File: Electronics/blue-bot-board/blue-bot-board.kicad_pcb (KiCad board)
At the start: 2 copper layers, 65 x 100 mm, 16 parts, among them J1 5V PS, J12 I2C0, J13 Extra GPIO, J2 X, J3 Y, J4 Z, J5 X Limit Switch, J6 Y Limit Switch, J7 Z Limit Switch, J8 Servo, SW1 RESET

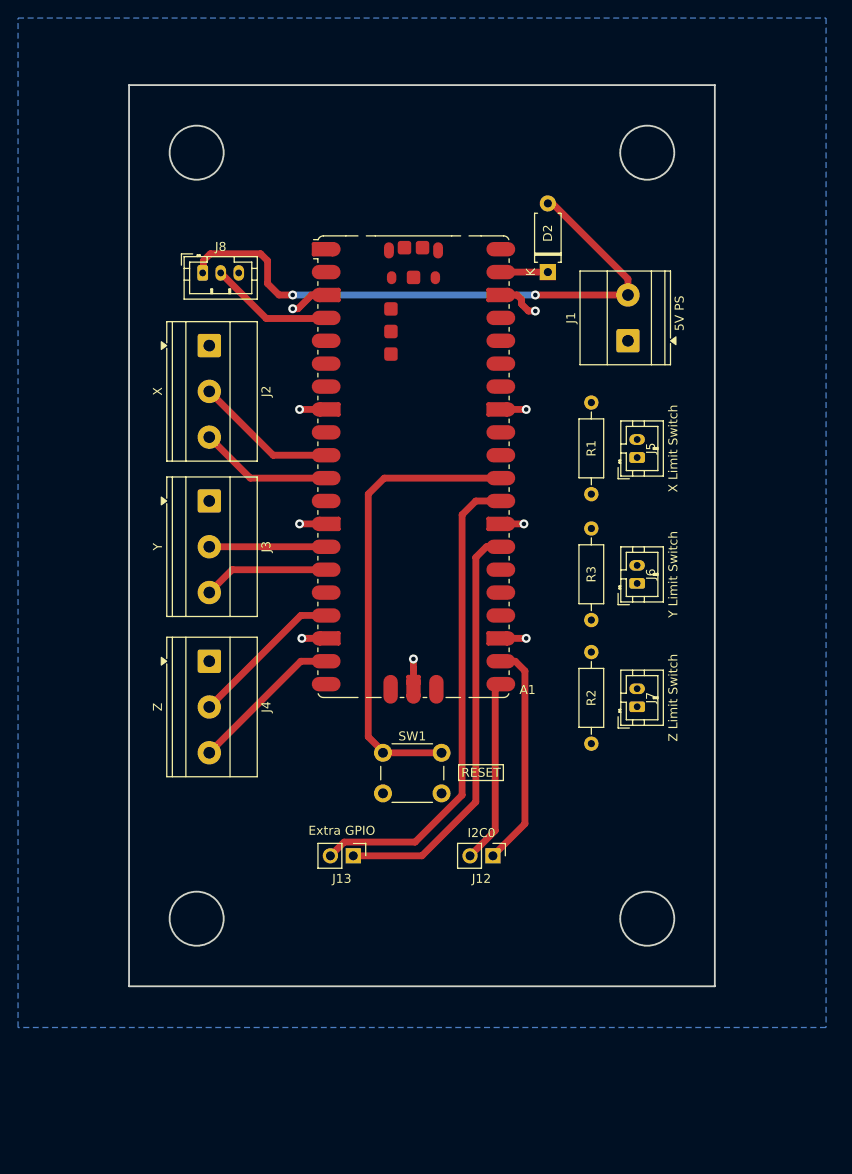
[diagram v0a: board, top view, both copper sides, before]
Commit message: Update PCB to production
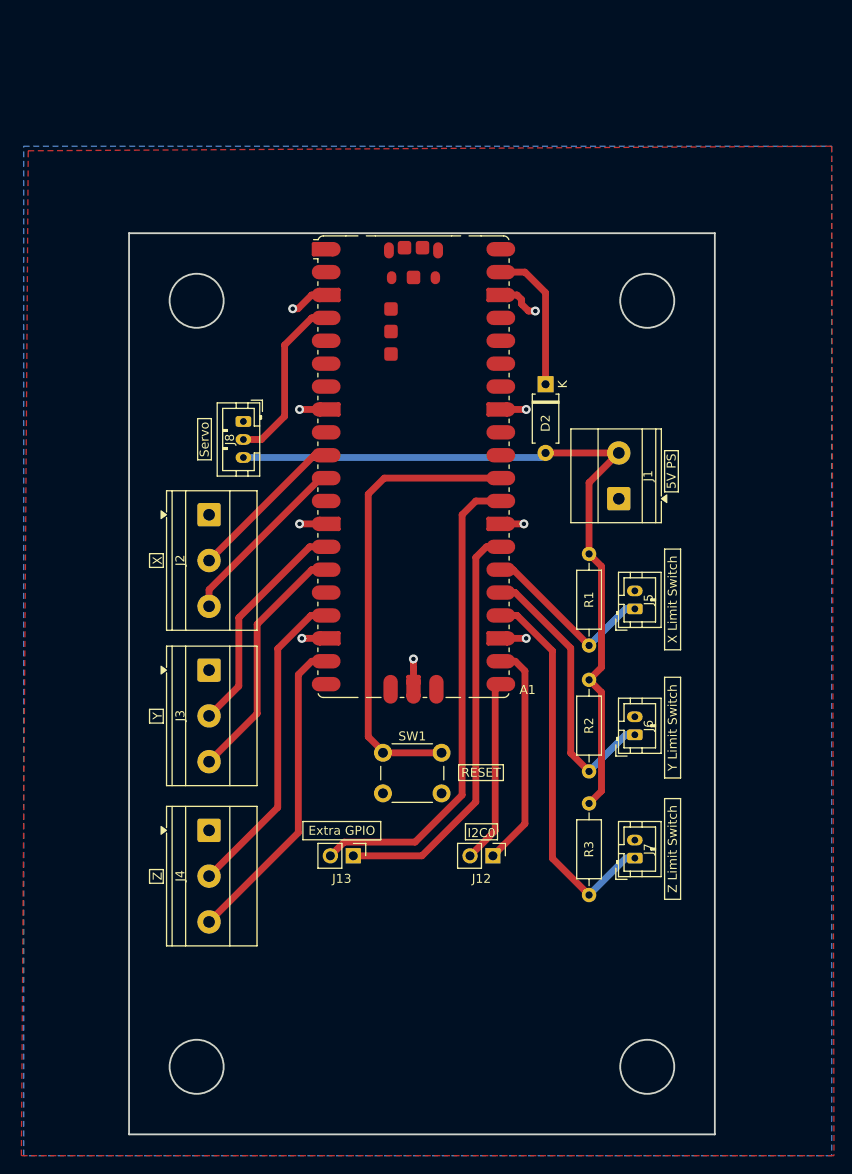
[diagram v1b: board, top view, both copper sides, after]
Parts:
- moved R3 30.5 mm to (164.1, 119.4)
- moved J2 18.8 mm to (121.9, 87.4)
- moved J3 18.8 mm to (121.9, 104.6)
- moved J4 18.8 mm to (121.9, 122.4)
- moved J1 17.6 mm to (167.4, 85.6)
- moved J8 17.1 mm to (125.7, 77.0), turned to -90 degrees
- moved J5 16.8 mm to (169.2, 97.8)
- moved J6 16.8 mm to (169.2, 111.8)
- moved J7 16.8 mm to (169.2, 125.5)
- moved R1 16.8 mm to (164.1, 91.7)
- moved D2 12.4 mm to (159.3, 72.9), turned to -90 degrees
- moved R2 3.09 mm to (164.1, 105.7)
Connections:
- J8 pad 1: +5V -> GND
- J8 pad 3: GND -> +5V
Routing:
- net Net-(A1-GPIO18): track 0.00 -> 42.9 mm
- net Net-(A1-GPIO19): track 0.00 -> 31.6 mm
- net Net-(A1-GPIO20): track 0.00 -> 20.0 mm
- net /GPIO13: track 17.2 -> 35.3 mm
- net /GPIO14: track 17.2 -> 35.2 mm
- net +5V: track 67.1 -> 84.4 mm, vias 2 -> 0
- net /GPIO11: track 14.0 -> 27.6 mm
- net /GPIO10: track 13.0 -> 25.2 mm
- net VCC: track 5.22 -> 16.4 mm
- net /GPIO2: track 13.8 -> 19.4 mm
- net /GPIO8: track 14.9 -> 20.4 mm
- net /GPIO7: track 15.9 -> 17.8 mm
- added copper zone on F.Cu, net GND
